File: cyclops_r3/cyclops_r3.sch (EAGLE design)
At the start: 108 parts, among them Q1 BC817, Q2 IRF510, U1 MCP4921, U2 MCP4022-50k, U3 317-N, U4 TLV3701, U5 337-N, U6 ADR03, U7 OP1177, U8 LTC2052HV, U9 ZXTD45

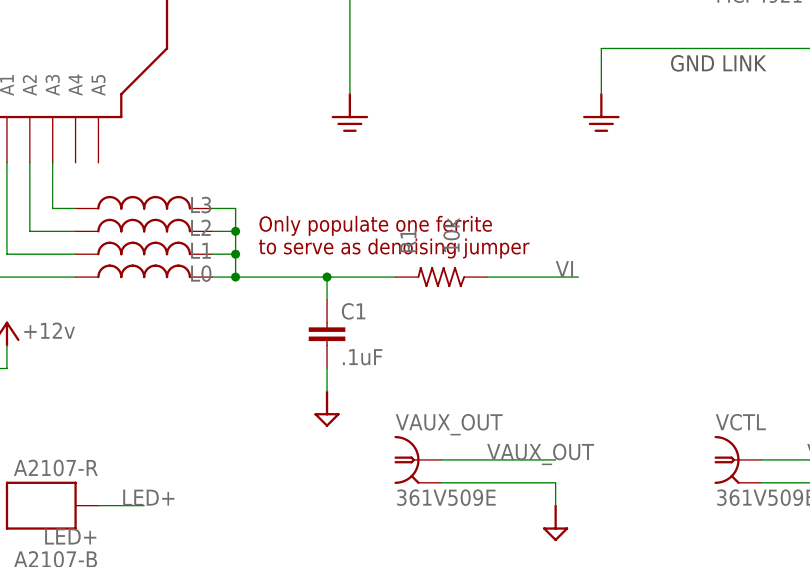
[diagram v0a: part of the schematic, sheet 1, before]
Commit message: Fixed most of the TODO issues. Need to rearrange front panel layout a bit to acomidate light pipes.
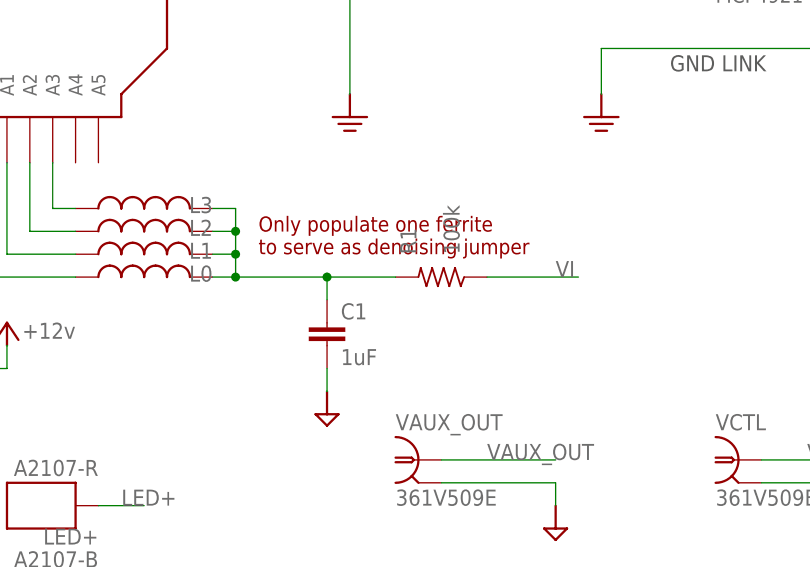
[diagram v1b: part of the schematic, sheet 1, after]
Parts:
- C1: value .1uF -> 1uF
- R1: value 10k -> 100k
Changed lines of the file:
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@@
 <part name="L1" library="cyclops" deviceset="L" device="_0603" value="MPZ1608"/>
 <part name="L0" library="cyclops" deviceset="L" device="_0603" value="MPZ1608"/>
-<part name="R1" library="cyclops" deviceset="R" device="_0603" value="10k"/>
-<part name="C1" library="cyclops" deviceset="C" device="_0603" value=".1uF"/>
+<part name="R1" library="cyclops" deviceset="R" device="_0603" value="100k"/>
+<part name="C1" library="cyclops" deviceset="C" device="_0603" value="1uF"/>
 <part name="U$50" library="cyclops" deviceset="GND2" device=""/>
 <part name="U$28" library="cyclops" deviceset="GND2" device=""/>

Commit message: Minor updates.
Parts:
- VCTL<->DAC: value 2M1 -> 2M1-SP3; device cyclops:SPDT_MTS-M6 -> cyclops:SPDT_2M-WITHOFF
- renumbered REF2.1 to REF2.5, REF5.1 to REF5.0
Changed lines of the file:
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@@
 <?xml version="1.0" encoding="utf-8"?>
 <!DOCTYPE eagle SYSTEM "eagle.dtd">
-<eagle version="6.5.0">
+<eagle version="6.4">
 <drawing>
 <settings>
@@
 <part name="R25" library="cyclops" deviceset="R" device="_0603" value="10"/>
 <part name="VAUX_OUT" library="cyclops" deviceset="BNC" device="_V-BITE" value="361V509E"/>
-<part name="REF2.1" library="cyclops" deviceset="TP" device="TP16R" value="TPTP16R"/>
-<part name="REF5.1" library="cyclops" deviceset="TP" device="TP16R" value="TPTP16R"/>
+<part name="REF2.5" library="cyclops" deviceset="TP" device="TP16R" value="TPTP16R"/>
+<part name="REF5.0" library="cyclops" deviceset="TP" device="TP16R" value="TPTP16R"/>
 <part name="VBIAS" library="cyclops" deviceset="TP" device="TP16R" value="TPTP16R"/>
 <part name="VGATE" library="cyclops" deviceset="TP" device="TP16R" value="TPTP16R"/>
@@
 <part name="PWR_IN" library="cyclops" deviceset="PINH1X3" device="_MINI-JR" value="PINH1X3_MINI-JR"/>
 <part name="GAIN" library="cyclops" deviceset="POT_US" device="_3310" value="1k"/>
-<part name="VCTL&lt;-&gt;DAC" library="cyclops" deviceset="SPDT" device="_MTS-M6" value="2M1"/>
+<part name="VCTL&lt;-&gt;DAC" library="cyclops" deviceset="SPDT" device="_2M-WITHOFF" value="2M1-SP3"/>
 <part name="L6" library="cyclops" deviceset="L" device="_0603" value="MPZ1608"/>
 <part name="L5" library="cyclops" deviceset="L" device="_0603" value="MPZ1608"/>
@@
 <instance part="C19" gate="C" x="-58.42" y="-106.68"/>
 <instance part="C17" gate="C" x="-73.66" y="-106.68"/>
-<instance part="REF2.1" gate="G$1" x="35.56" y="5.08"/>
-<instance part="REF5.1" gate="G$1" x="45.72" y="-81.28"/>
+<instance part="REF2.5" gate="G$1" x="35.56" y="5.08"/>
+<instance part="REF5.0" gate="G$1" x="45.72" y="-81.28"/>
 <instance part="U$1" gate="G$1" x="-73.66" y="-154.94"/>
 <instance part="U$2" gate="G$1" x="-58.42" y="-154.94"/>
@@
 <junction x="35.56" y="2.54"/>
 <label x="53.34" y="2.54" size="1.778" layer="95"/>
-<pinref part="REF2.1" gate="G$1" pin="TP"/>
+<pinref part="REF2.5" gate="G$1" pin="TP"/>
 </segment>
 <segment>
@@
 <junction x="45.72" y="-83.82"/>
 <label x="66.04" y="-83.82" size="1.778" layer="95"/>
-<pinref part="REF5.1" gate="G$1" pin="TP"/>
-</segment>
-</net>
+<pinref part="REF5.0" gate="G$1" pin="TP"/>
+</segment>
+</net>

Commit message: Some minor fixes.
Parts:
- VCTL<->DAC: value 2M1-SP3 -> 100-SP3
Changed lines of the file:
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@@
 <part name="PWR_IN" library="cyclops" deviceset="PINH1X3" device="_MINI-JR" value="PINH1X3_MINI-JR"/>
 <part name="GAIN" library="cyclops" deviceset="POT_US" device="_3310" value="1k"/>
-<part name="VCTL&lt;-&gt;DAC" library="cyclops" deviceset="SPDT" device="_2M-WITHOFF" value="2M1-SP3"/>
+<part name="VCTL&lt;-&gt;DAC" library="cyclops" deviceset="SPDT" device="_2M-WITHOFF" value="100-SP3"/>
 <part name="L6" library="cyclops" deviceset="L" device="_0603" value="MPZ1608"/>
 <part name="L5" library="cyclops" deviceset="L" device="_0603" value="MPZ1608"/>

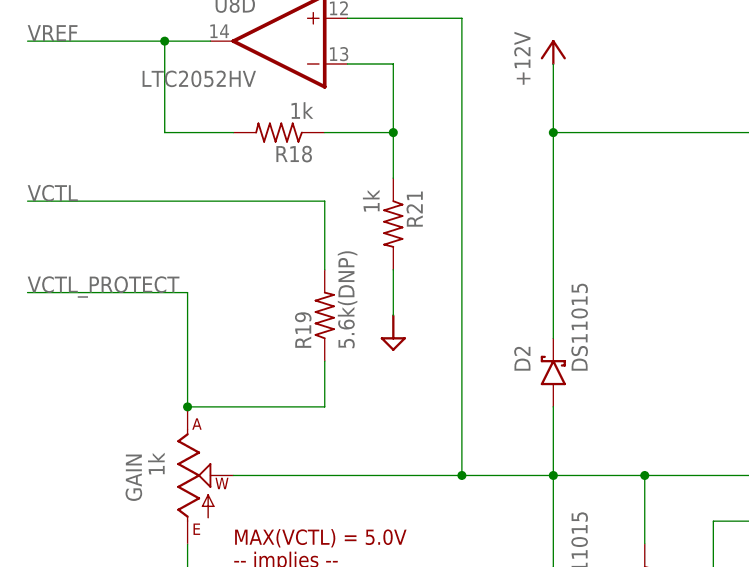
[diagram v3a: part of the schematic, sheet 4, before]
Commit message: Some layout changes to make ergonomic. Updated BOM.
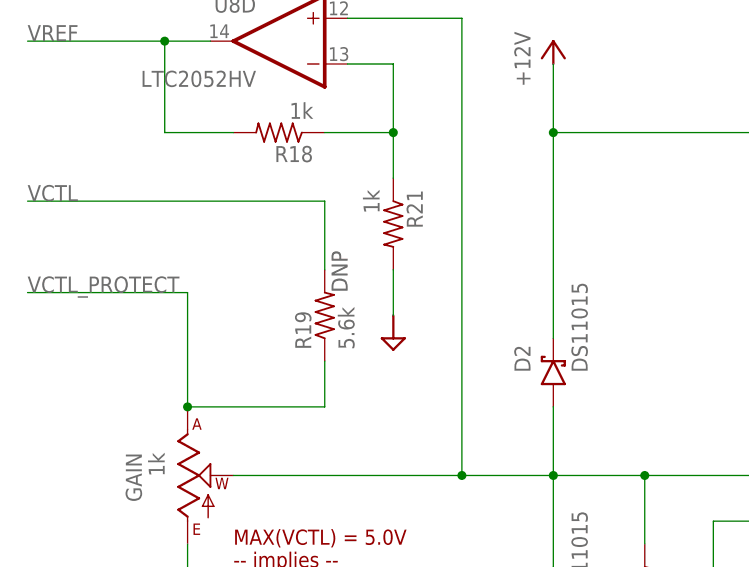
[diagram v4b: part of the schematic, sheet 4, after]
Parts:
- R19: value 5.6k(DNP) -> 5.6k
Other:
- note added: "DNP"
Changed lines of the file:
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@@
 <?xml version="1.0" encoding="utf-8"?>
 <!DOCTYPE eagle SYSTEM "eagle.dtd">
-<eagle version="6.4">
+<eagle version="6.5.0">
 <drawing>
 <settings>
@@
 <setting verticaltext="up"/>
 </settings>
-<grid distance="0.1" unitdist="inch" unit="inch" style="lines" multiple="1" display="no" altdistance="0.01" altunitdist="inch" altunit="inch"/>
+<grid distance="0.05" unitdist="inch" unit="inch" style="lines" multiple="1" display="no" altdistance="0.01" altunitdist="inch" altunit="inch"/>
 <layers>
 <layer number="1" name="Top" color="4" fill="1" visible="no" active="no"/>
@@
 <part name="U$42" library="cyclops" deviceset="GND2" device=""/>
 <part name="U$43" library="cyclops" deviceset="GND2" device=""/>
-<part name="R19" library="cyclops" deviceset="R" device="_0603" value="5.6k(DNP)"/>
+<part name="R19" library="cyclops" deviceset="R" device="_0603" value="5.6k"/>
 <part name="U$45" library="cyclops" deviceset="GND2" device=""/>
 <part name="P+4" library="cyclops" deviceset="+5V" device="" value="+12V"/>
@@
 Max(ILED) ~ 1.5 Amps</text>
 <text x="-68.58" y="-5.08" size="1.6764" layer="94">VI = 1A/1V</text>
+<text x="-33.02" y="106.68" size="1.778" layer="97" rot="R90">DNP</text>
 </plain>
 <instances>

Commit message: Minor.
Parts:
- renumbered VCTL<->DAC to VCTL<OFF>DAC
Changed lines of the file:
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@@
 <part name="PWR_IN" library="cyclops" deviceset="PINH1X3" device="_MINI-JR" value="PINH1X3_MINI-JR"/>
 <part name="GAIN" library="cyclops" deviceset="POT_US" device="_3310" value="1k"/>
-<part name="VCTL&lt;-&gt;DAC" library="cyclops" deviceset="SPDT" device="_2M-WITHOFF" value="100-SP3"/>
+<part name="VCTL&lt;OFF&gt;DAC" library="cyclops" deviceset="SPDT" device="_2M-WITHOFF" value="100-SP3"/>
 <part name="L6" library="cyclops" deviceset="L" device="_0603" value="MPZ1608"/>
 <part name="L5" library="cyclops" deviceset="L" device="_0603" value="MPZ1608"/>
@@
 <instance part="PWR_DIST" gate="G$1" x="33.02" y="-20.32"/>
 <instance part="PWR_IN" gate="G$1" x="25.4" y="5.08"/>
-<instance part="VCTL&lt;-&gt;DAC" gate="G$1" x="193.04" y="17.78" rot="MR0"/>
+<instance part="VCTL&lt;OFF&gt;DAC" gate="G$1" x="193.04" y="17.78" rot="MR0"/>
 <instance part="L6" gate="L" x="53.34" y="38.1" smashed="yes">
 <attribute name="NAME" x="52.07" y="30.48" size="1.778" layer="95" rot="R90"/>
@@
 <wire x1="172.72" y1="78.74" x2="172.72" y2="81.28" width="0.1524" layer="91"/>
 <junction x="172.72" y="81.28"/>
-<pinref part="VCTL&lt;-&gt;DAC" gate="G$1" pin="1"/>
+<pinref part="VCTL&lt;OFF&gt;DAC" gate="G$1" pin="1"/>
 <wire x1="180.34" y1="20.32" x2="185.42" y2="20.32" width="0.1524" layer="91"/>
 <wire x1="180.34" y1="81.28" x2="180.34" y2="20.32" width="0.1524" layer="91"/>
@@
 <pinref part="VCTL" gate="G$1" pin="1"/>
 <label x="152.4" y="15.24" size="1.778" layer="95"/>
-<pinref part="VCTL&lt;-&gt;DAC" gate="G$1" pin="3"/>
+<pinref part="VCTL&lt;OFF&gt;DAC" gate="G$1" pin="3"/>
 <wire x1="185.42" y1="15.24" x2="147.32" y2="15.24" width="0.1524" layer="91"/>
 </segment>
@@
 <wire x1="195.58" y1="17.78" x2="203.2" y2="17.78" width="0.1524" layer="91"/>
 <pinref part="TEST" gate="G$1" pin="1"/>
-<pinref part="VCTL&lt;-&gt;DAC" gate="G$1" pin="2"/>
-</segment>
-</net>
+<pinref part="VCTL&lt;OFF&gt;DAC" gate="G$1" pin="2"/>
+</segment>
+</net>

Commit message: BOM update.
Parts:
- COMP, OC: value LEDRED -> RED
- PWR: value LEDGRN -> BLUE
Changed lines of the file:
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@@
 <part name="VGATE" library="cyclops" deviceset="TP" device="TP16R" value="TPTP16R"/>
 <part name="R9" library="cyclops" deviceset="R" device="_0603" value="3k"/>
-<part name="PWR" library="cyclops" deviceset="LED" device="_0603" value="LEDGRN"/>
+<part name="PWR" library="cyclops" deviceset="LED" device="_0603" value="BLUE"/>
 <part name="U4" library="ti-extended" deviceset="TLV3701CDBVT" device="" value="TLV3701"/>
 <part name="R5" library="cyclops" deviceset="R" device="_0603" value="10k"/>
@@
 <part name="C10" library="cyclops" deviceset="C" device="_0603" value=".1uF"/>
 <part name="R10" library="cyclops" deviceset="R" device="_0603" value="1k"/>
-<part name="OC" library="cyclops" deviceset="LED" device="_0603" value="LEDRED"/>
+<part name="OC" library="cyclops" deviceset="LED" device="_0603" value="RED"/>
 <part name="C8" library="cyclops" deviceset="C" device="_0603" value=".1uF"/>
 <part name="U5" library="cyclops" deviceset="*337" device="IMP" value="337-N"/>
@@
 <part name="C6" library="cyclops" deviceset="C" device="_0603" value=".1uF"/>
 <part name="R11" library="cyclops" deviceset="R" device="_0603" value="1k"/>
-<part name="COMP" library="cyclops" deviceset="LED" device="_0603" value="LEDRED"/>
+<part name="COMP" library="cyclops" deviceset="LED" device="_0603" value="RED"/>
 <part name="U$49" library="cyclops" deviceset="GND2" device=""/>
 <part name="L3" library="cyclops" deviceset="L" device="_0603" value="MPZ1608"/>

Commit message: Minor.
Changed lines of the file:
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@@
 <setting verticaltext="up"/>
 </settings>
-<grid distance="0.05" unitdist="inch" unit="inch" style="lines" multiple="1" display="no" altdistance="0.01" altunitdist="inch" altunit="inch"/>
+<grid distance="0.1" unitdist="inch" unit="inch" style="lines" multiple="1" display="no" altdistance="0.01" altunitdist="inch" altunit="inch"/>
 <layers>
 <layer number="1" name="Top" color="4" fill="1" visible="no" active="no"/>
@@
 <part name="U$27" library="cyclops" deviceset="GND2" device=""/>
 <part name="U$29" library="cyclops" deviceset="GND2" device=""/>
-<part name="P-1" library="cyclops" deviceset="-5V" device="" value="-2.1V"/>
+<part name="P-1" library="cyclops" deviceset="-5V" device="" value="-1.25V"/>
 <part name="P+1" library="cyclops" deviceset="+5V" device="" value="+5V"/>
 <part name="P+2" library="cyclops" deviceset="+5V" device="" value="+5V"/>
@@
 <part name="U$20" library="cyclops" deviceset="GND2" device=""/>
 <part name="R22" library="cyclops" deviceset="R" device="_0603" value="220k"/>
-<part name="P-2" library="cyclops" deviceset="-5V" device="" value="-2.1V"/>
+<part name="P-2" library="cyclops" deviceset="-5V" device="" value="-1.25V"/>
 <part name="P+5" library="cyclops" deviceset="+5V" device="" value="+12V"/>
 <part name="R20" library="cyclops" deviceset="R" device="_0603" value="220k"/>

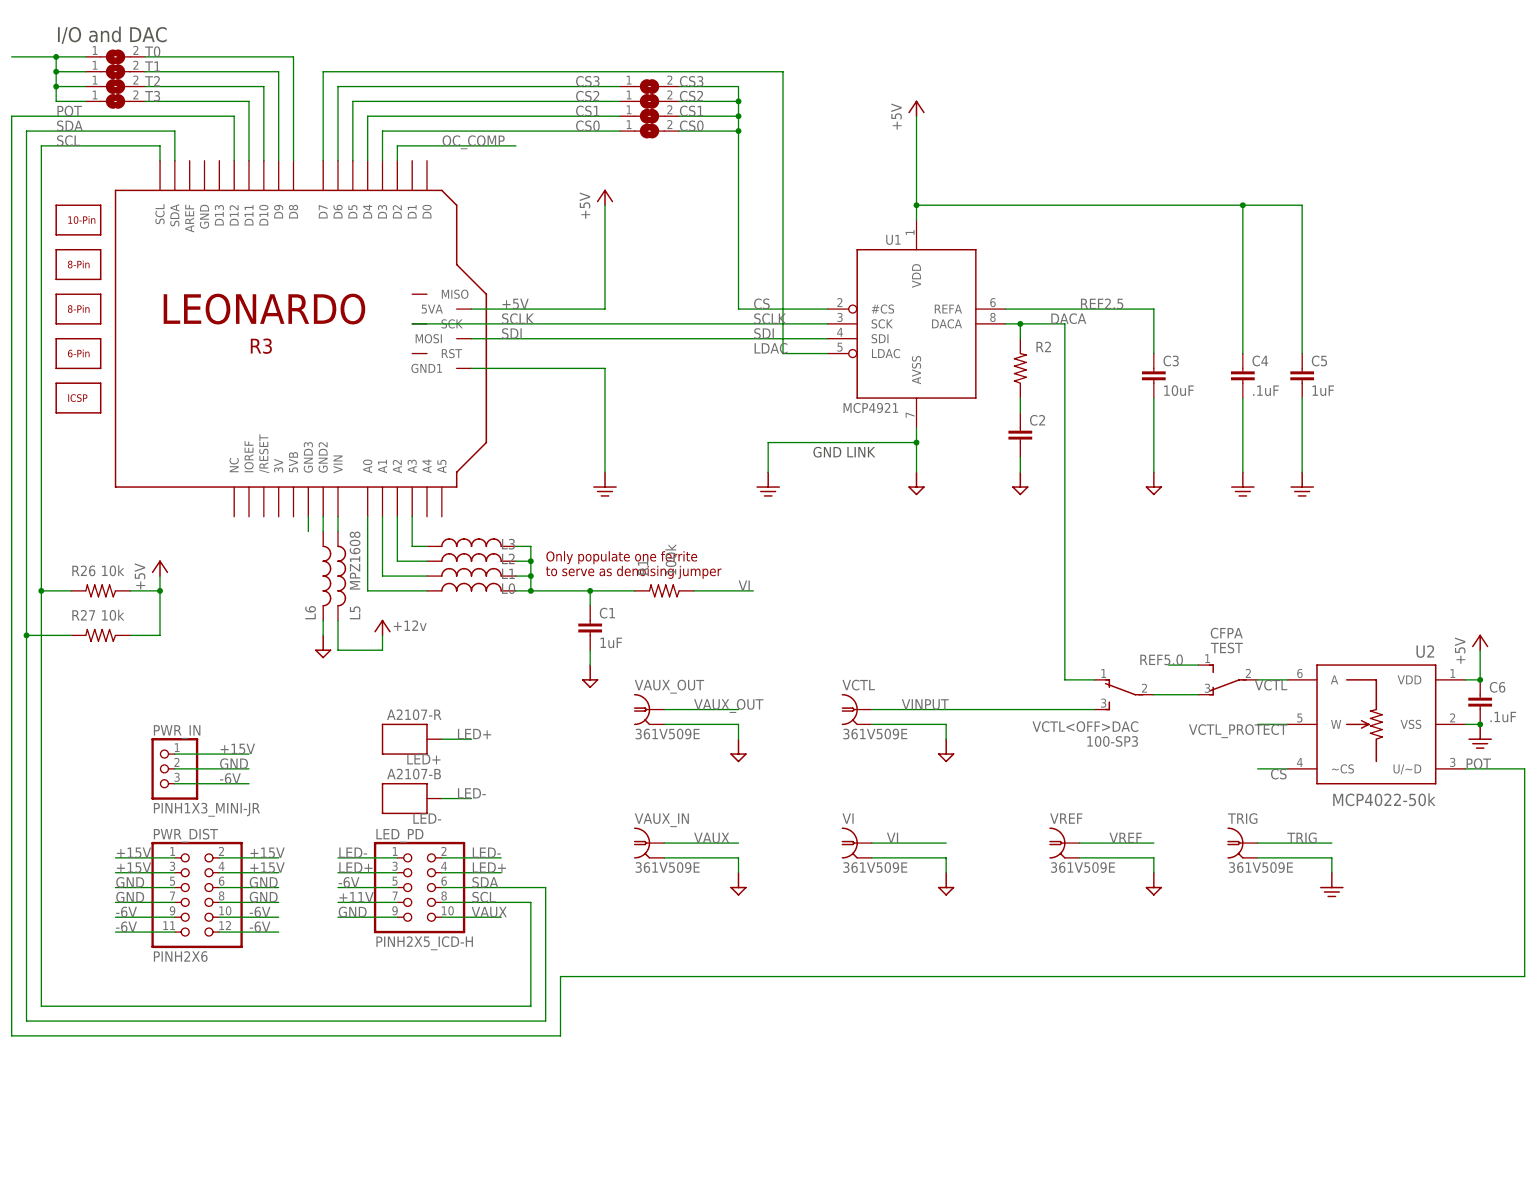
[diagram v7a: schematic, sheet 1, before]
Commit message: Added automatic logic level conversion on trigger line.
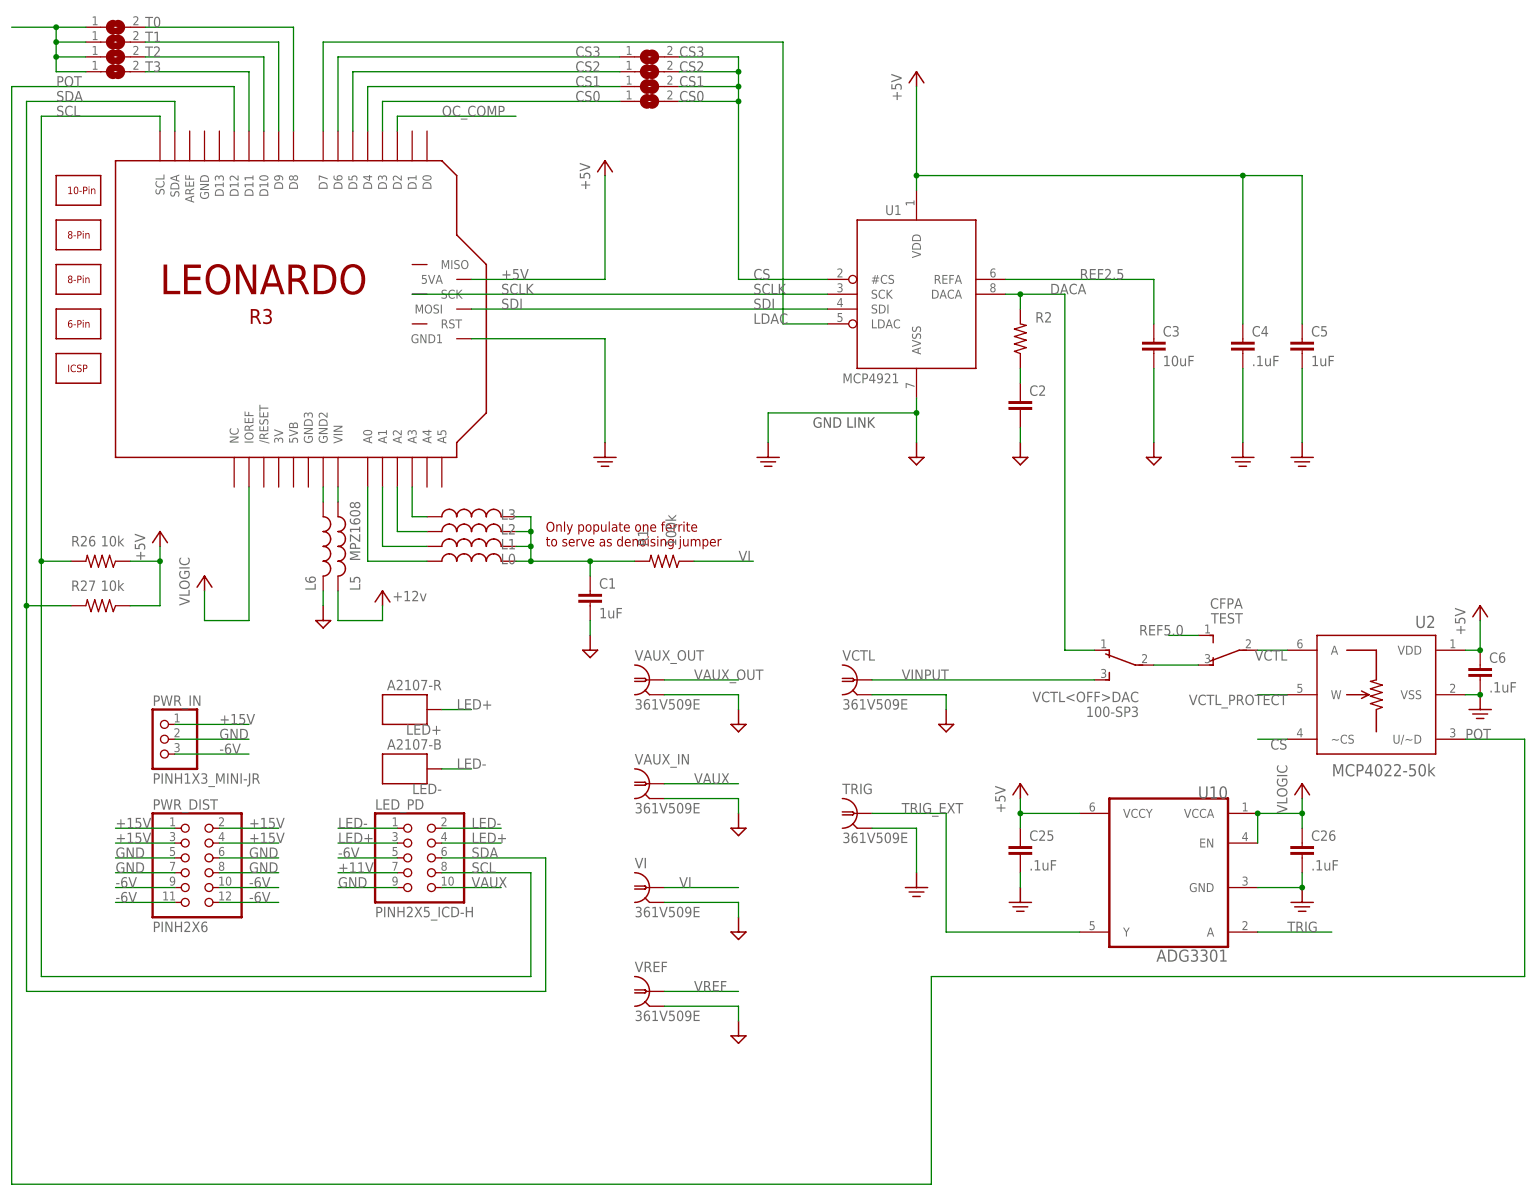
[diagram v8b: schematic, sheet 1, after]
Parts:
- added C25, C26: .1uF, cyclops:C_0603
- added U10: ADG3301, cyclops:ADG3301BKSZ-REEL
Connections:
- new net TRIG_EXT: TRIG.1, U10.Y
- new net VLOGIC: C26.1, LEONARDO.IOREF, U10.EN, U10.VCCA
- net +5V: now also C25.1, U10.VCCY
- net GND: now also C25.2, C26.2, U10.GND
- net KEEPOUT_GND: no longer LEONARDO.GND3
- net TRIG: now also U10.A; no longer TRIG.1
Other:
- note removed: "I/O and DAC"
- moved on the sheet: C1, C2, C3, C4, C5, C6, CS0, CS1, CS2, CS3, L0, L1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
